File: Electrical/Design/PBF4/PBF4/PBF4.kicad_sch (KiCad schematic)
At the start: 0 parts

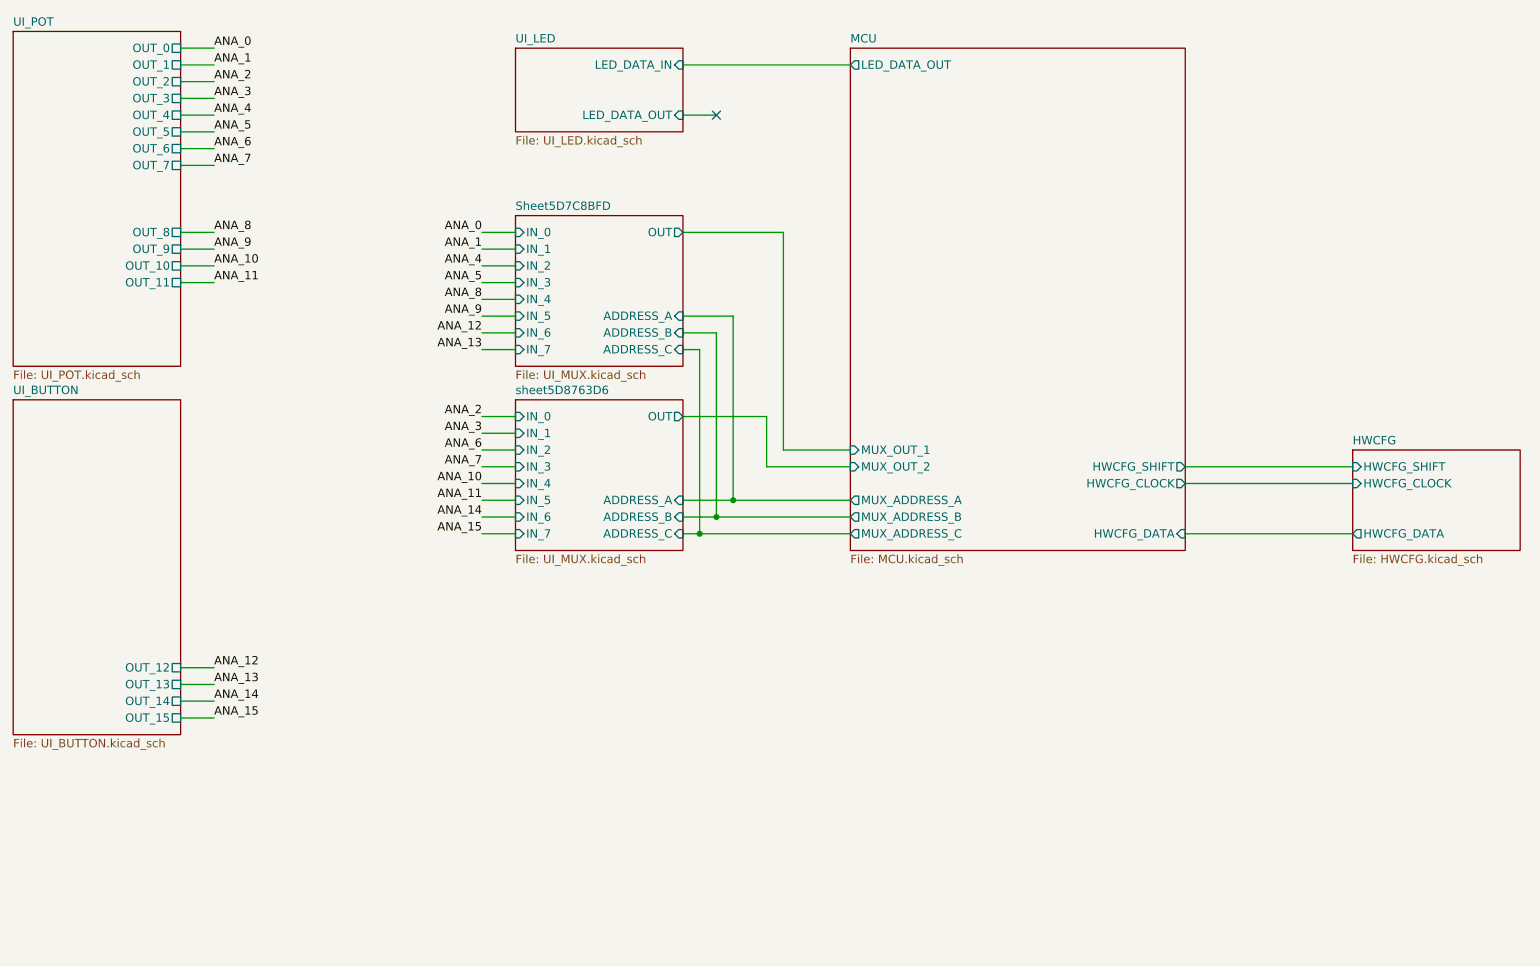
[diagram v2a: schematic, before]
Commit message: SUKU PBF4 ESP32 migration routing done, ERC DRC checked
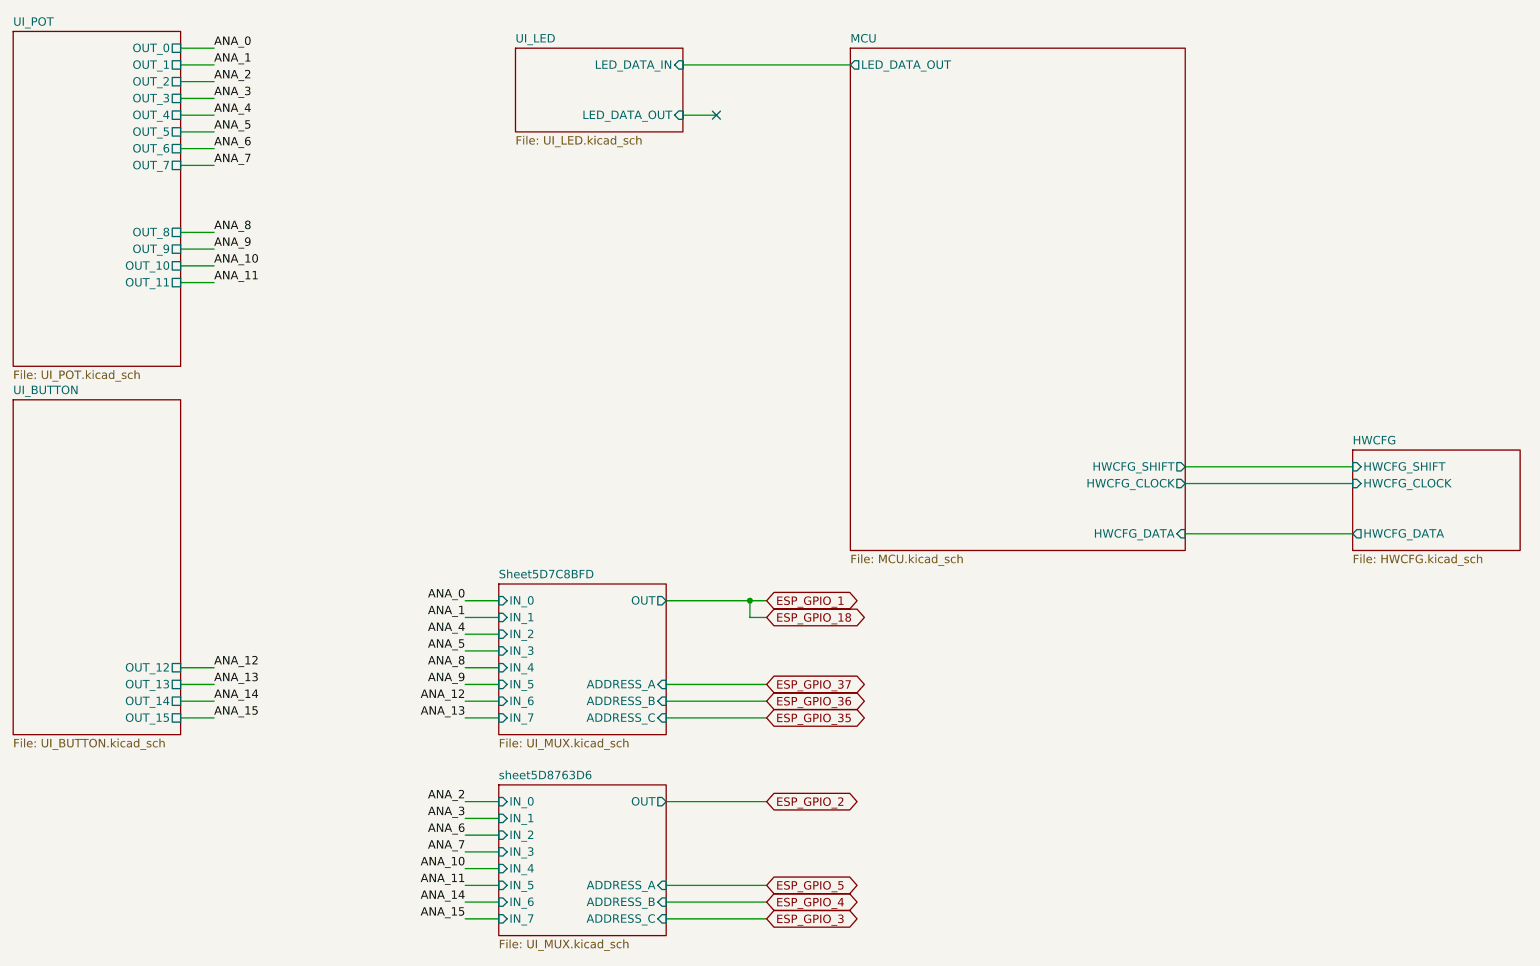
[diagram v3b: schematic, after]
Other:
- sheet MCU ports: added none; removed MUX_ADDRESS_A, MUX_ADDRESS_B, MUX_ADDRESS_C, MUX_OUT_1, MUX_OUT_2
